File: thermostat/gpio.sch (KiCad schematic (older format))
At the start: 24 parts, among them J5 Conn_01x20, Q4 BC817, Q5 BC817, Q6 BC817, U8 PCF8574

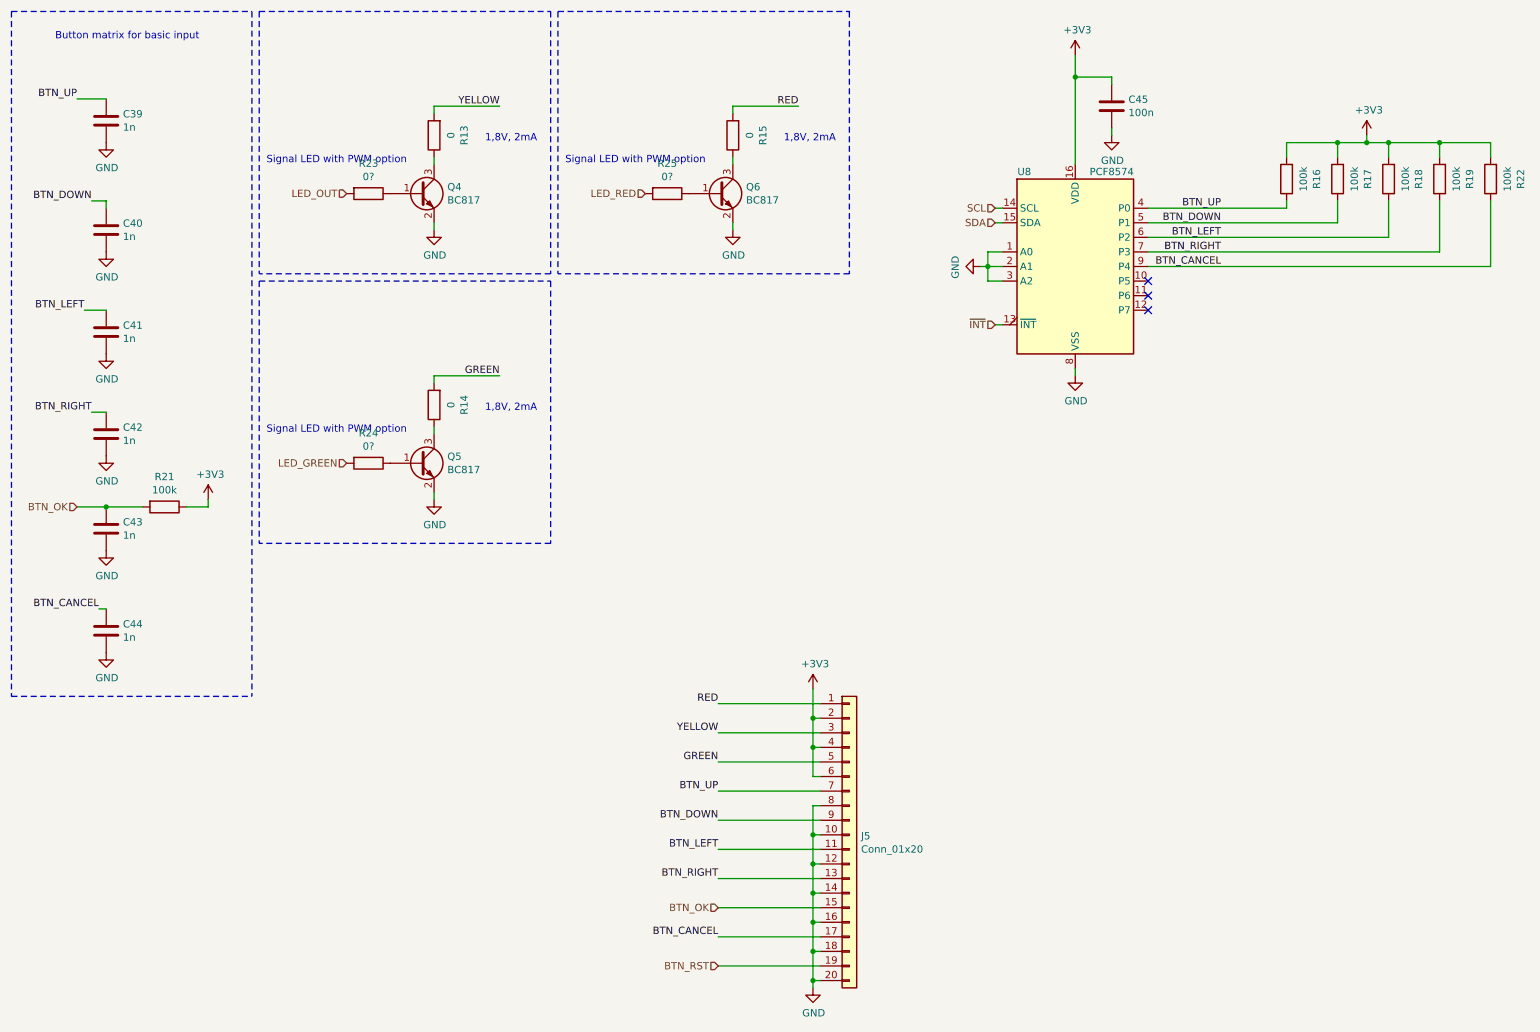
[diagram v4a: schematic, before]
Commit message: Changed LED and regulator_out drivers to NMOS instead of bipolar. Started routing, SPI and I2C lines done.
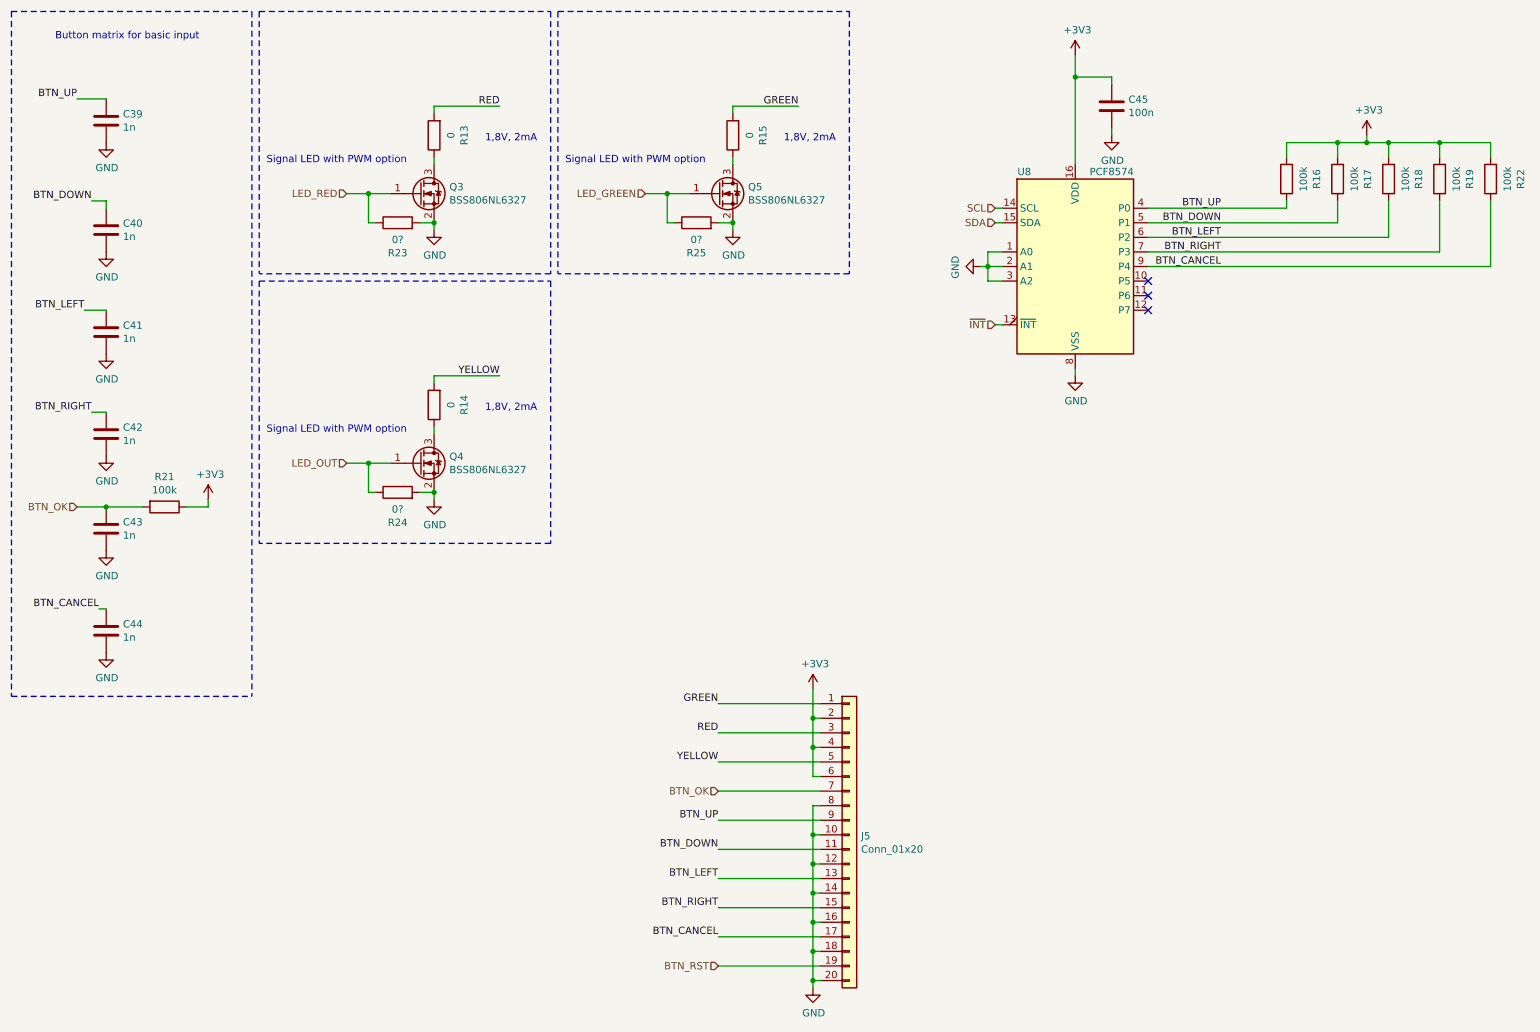
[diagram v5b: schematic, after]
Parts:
- removed Q4, Q5, Q6: BC817, Package_TO_SOT_SMD:SOT-23, symbol Device:Q_NPN_BEC
- added Q3, Q4, Q5: BSS806NL6327, Package_TO_SOT_SMD:SOT-23, symbol Device:Q_NMOS_GSD
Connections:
- net BTN_DOWN: now also J5.11 (Pin_11); no longer J5.9 (Pin_9)
- net BTN_LEFT: now also J5.13 (Pin_13); no longer J5.11 (Pin_11)
- net BTN_OK: now also J5.7 (Pin_7); no longer J5.15 (Pin_15)
- net BTN_RIGHT: now also J5.15 (Pin_15); no longer J5.13 (Pin_13)
- net BTN_UP: now also J5.9 (Pin_9); no longer J5.7 (Pin_7)
- net GND: now also R23.2, R24.2, R25.2, Q3.2 (S), Q4.2 (S), Q5.2 (S)
- net GREEN: now also J5.1 (Pin_1), R15.2; no longer J5.5 (Pin_5), R14.2
- net LED_GREEN: now also R25.1, Q5.1 (G); no longer R24.2
- net LED_OUT: now also R24.1, Q4.1 (G); no longer R23.2
- net LED_RED: now also R23.1, Q3.1 (G); no longer R25.2
- net RED: now also J5.3 (Pin_3), R13.2; no longer J5.1 (Pin_1), R15.2
- net YELLOW: now also J5.5 (Pin_5), R14.2; no longer J5.3 (Pin_3), R13.2
- net at R15.1: now also Q5.3 (D)
- net at R13.1: now also Q3.3 (D)
- net at R14.1: now also Q4.3 (D)
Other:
- moved on the sheet: R23, R24, R25
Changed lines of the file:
@@
 Text Notes 5950 1500 0    50   ~ 0
 1,8V, 2mA
-$Comp
-L Device:Q_NPN_BEC Q?
-U 1 1 5F3B8DF8
-P 5500 1850
-AR Path="/5E6A63AE/5F3B8DF8" Ref="Q?"  Part="1"
-AR Path="/5F3B8DF8" Ref="Q?"  Part="1"
-AR Path="/5F39C8C1/5F3B8DF8" Ref="Q6"  Part="1"
-F 0 "Q6" H 5691 1896 50  0000 L CNN
-F 1 "BC817" H 5691 1805 50  0000 L CNN
-F 2 "Package_TO_SOT_SMD:SOT-23" H 5700 1950 50  0001 C CNN
-F 3 "https://www.mouser.de/datasheet/2/916/BC817_SER-1598763.pdf" H 5500 1850 50  0001 C CNN
-	1    5500 1850
-	1    0    0    -1
-$EndComp
 Wire Wire Line
 	5600 1600 5600 1650
@@
 Text Notes 3900 1500 0    50   ~ 0
 1,8V, 2mA
-$Comp
-L Device:Q_NPN_BEC Q?
-U 1 1 5F3B8E17
-P 3450 1850
-AR Path="/5E6A63AE/5F3B8E17" Ref="Q?"  Part="1"
-AR Path="/5F3B8E17" Ref="Q?"  Part="1"
-AR Path="/5F39C8C1/5F3B8E17" Ref="Q4"  Part="1"
-F 0 "Q4" H 3641 1896 50  0000 L CNN
-F 1 "BC817" H 3641 1805 50  0000 L CNN
-F 2 "Package_TO_SOT_SMD:SOT-23" H 3650 1950 50  0001 C CNN
-F 3 "https://www.mouser.de/datasheet/2/916/BC817_SER-1598763.pdf" H 3450 1850 50  0001 C CNN
-	1    3450 1850
-	1    0    0    -1
-$EndComp
 Wire Wire Line
 	3550 1600 3550 1650
@@
 Text Notes 3900 3350 0    50   ~ 0
 1,8V, 2mA
-$Comp
-L Device:Q_NPN_BEC Q?
-U 1 1 5F3B8E36
-P 3450 3700
-AR Path="/5E6A63AE/5F3B8E36" Ref="Q?"  Part="1"
-AR Path="/5F3B8E36" Ref="Q?"  Part="1"
-AR Path="/5F39C8C1/5F3B8E36" Ref="Q5"  Part="1"
-F 0 "Q5" H 3641 3746 50  0000 L CNN
-F 1 "BC817" H 3641 3655 50  0000 L CNN
-F 2 "Package_TO_SOT_SMD:SOT-23" H 3650 3800 50  0001 C CNN
-F 3 "https://www.mouser.de/datasheet/2/916/BC817_SER-1598763.pdf" H 3450 3700 50  0001 C CNN
-	1    3450 3700
-	1    0    0    -1
-$EndComp
 Wire Wire Line
 	3550 3450 3550 3500
@@
 Wire Notes Line
 	2350 600  2350 2400
+Text HLabel 2950 3700 0    50   Input ~ 0
+LED_OUT
 Text HLabel 2950 1850 0    50   Input ~ 0
-LED_OUT
+LED_RED
 Text HLabel 5000 1850 0    50   Input ~ 0
-LED_RED
-Text HLabel 2950 3700 0    50   Input ~ 0
 LED_GREEN
 Text Label 1100 1200 2    50   ~ 0
@@
 Wire Wire Line
 	5500 7150 6200 7150
+Text Label 5500 6750 2    50   ~ 0
+BTN_RIGHT
 Text Label 5500 6550 2    50   ~ 0
-BTN_RIGHT
+BTN_LEFT
 Text Label 5500 6350 2    50   ~ 0
-BTN_LEFT
+BTN_DOWN
 Text Label 5500 6150 2    50   ~ 0
-BTN_DOWN
-Text Label 5500 5950 2    50   ~ 0
 BTN_UP
 Text HLabel 5500 7150 0    50   Input ~ 0
@@
 Wire Wire Line
 	6200 5350 5500 5350
+Text Label 5500 5350 2    50   ~ 0
+GREEN
 Text Label 5500 5750 2    50   ~ 0
-GREEN
+YELLOW
 Text Label 5500 5550 2    50   ~ 0
-YELLOW
-Text Label 5500 5350 2    50   ~ 0
 RED
 $Comp
@@
 Wire Wire Line
 	3550 3100 4000 3100
+Text Label 4000 1250 2    50   ~ 0
+RED
+Text Label 4000 3100 2    50   ~ 0
+YELLOW
 Text Label 6050 1250 2    50   ~ 0
-RED
-Text Label 4000 1250 2    50   ~ 0
-YELLOW
-Text Label 4000 3100 2    50   ~ 0
 GREEN
 $Comp
@@
 Text HLabel 1100 4000 0    50   Input ~ 0
 BTN_OK
-Text HLabel 5500 6750 0    50   Input ~ 0
+Text HLabel 5500 5950 0    50   Input ~ 0
 BTN_OK
 Text Label 5500 6950 2    50   ~ 0
@@
 L Device:R R?
 U 1 1 5FAA9C4A
-P 3100 1850
+P 3300 2050
 AR Path="/5E6A63AE/5FAA9C4A" Ref="R?"  Part="1"
 AR Path="/5FAA9C4A" Ref="R?"  Part="1"
 AR Path="/5F39C8C1/5FAA9C4A" Ref="R23"  Part="1"
-F 0 "R23" V 2893 1850 50  0000 C CNN
-F 1 "0?" V 2984 1850 50  0000 C CNN
-F 2 "Resistor_SMD:R_0402_1005Metric" V 3030 1850 50  0001 C CNN
-F 3 "~" H 3100 1850 50  0001 C CNN
-	1    3100 1850
-	0    1    1    0
+F 0 "R23" V 3093 2050 50  0000 C CNN
+F 1 "0?" V 3184 2050 50  0000 C CNN
+F 2 "Resistor_SMD:R_0402_1005Metric" V 3230 2050 50  0001 C CNN
+F 3 "~" H 3300 2050 50  0001 C CNN
+	1    3300 2050
+	0    -1   -1   0
 $EndComp
 $Comp
 L Device:R R?
 U 1 1 5FAAA4F5
-P 5150 1850
+P 5350 2050
 AR Path="/5E6A63AE/5FAAA4F5" Ref="R?"  Part="1"
 AR Path="/5FAAA4F5" Ref="R?"  Part="1"
 AR Path="/5F39C8C1/5FAAA4F5" Ref="R25"  Part="1"
-F 0 "R25" V 4943 1850 50  0000 C CNN
-F 1 "0?" V 5034 1850 50  0000 C CNN
-F 2 "Resistor_SMD:R_0402_1005Metric" V 5080 1850 50  0001 C CNN
-F 3 "~" H 5150 1850 50  0001 C CNN
-	1    5150 1850
-	0    1    1    0
+F 0 "R25" V 5143 2050 50  0000 C CNN
+F 1 "0?" V 5234 2050 50  0000 C CNN
+F 2 "Resistor_SMD:R_0402_1005Metric" V 5280 2050 50  0001 C CNN
+F 3 "~" H 5350 2050 50  0001 C CNN
+	1    5350 2050
+	0    -1   -1   0
 $EndComp
 $Comp
 L Device:R R?
 U 1 1 5FAAA7FD
-P 3100 3700
+P 3300 3900
 AR Path="/5E6A63AE/5FAAA7FD" Ref="R?"  Part="1"
 AR Path="/5FAAA7FD" Ref="R?"  Part="1"
 AR Path="/5F39C8C1/5FAAA7FD" Ref="R24"  Part="1"
-F 0 "R24" V 2893 3700 50  0000 C CNN
-F 1 "0?" V 2984 3700 50  0000 C CNN
-F 2 "Resistor_SMD:R_0402_1005Metric" V 3030 3700 50  0001 C CNN
-F 3 "~" H 3100 3700 50  0001 C CNN
-	1    3100 3700
-	0    1    1    0
-$EndComp
+F 0 "R24" V 3093 3900 50  0000 C CNN
+F 1 "0?" V 3184 3900 50  0000 C CNN
+F 2 "Resistor_SMD:R_0402_1005Metric" V 3230 3900 50  0001 C CNN
+F 3 "~" H 3300 3900 50  0001 C CNN
+	1    3300 3900
+	0    -1   -1   0
+$EndComp
+$Comp
+L Device:Q_NMOS_GSD Q?
+U 1 1 5F792335
+P 3450 1850
+AR Path="/5E63CFCA/5F792335" Ref="Q?"  Part="1"
+AR Path="/5F792335" Ref="Q?"  Part="1"
+AR Path="/5F306ECC/5F792335" Ref="Q?"  Part="1"
+AR Path="/5F39C8C1/5F792335" Ref="Q3"  Part="1"
+F 0 "Q3" H 3655 1896 50  0000 L CNN
+F 1 "BSS806NL6327" H 3655 1805 50  0000 L CNN
+F 2 "Package_TO_SOT_SMD:SOT-23" H 3650 1950 50  0001 C CNN
+F 3 "~" H 3450 1850 50  0001 C CNN
+	1    3450 1850
+	1    0    0    -1
+$EndComp
+$Comp
+L Device:Q_NMOS_GSD Q?
+U 1 1 5F7963CB
+P 3450 3700
+AR Path="/5E63CFCA/5F7963CB" Ref="Q?"  Part="1"
+AR Path="/5F7963CB" Ref="Q?"  Part="1"
+AR Path="/5F306ECC/5F7963CB" Ref="Q?"  Part="1"
+AR Path="/5F39C8C1/5F7963CB" Ref="Q4"  Part="1"
+F 0 "Q4" H 3655 3746 50  0000 L CNN
+F 1 "BSS806NL6327" H 3655 3655 50  0000 L CNN
+F 2 "Package_TO_SOT_SMD:SOT-23" H 3650 3800 50  0001 C CNN
+F 3 "~" H 3450 3700 50  0001 C CNN
+	1    3450 3700
+	1    0    0    -1
+$EndComp
+$Comp
+L Device:Q_NMOS_GSD Q?
+U 1 1 5F796F73
+P 5500 1850
+AR Path="/5E63CFCA/5F796F73" Ref="Q?"  Part="1"
+AR Path="/5F796F73" Ref="Q?"  Part="1"
+AR Path="/5F306ECC/5F796F73" Ref="Q?"  Part="1"
+AR Path="/5F39C8C1/5F796F73" Ref="Q5"  Part="1"
+F 0 "Q5" H 5705 1896 50  0000 L CNN
+F 1 "BSS806NL6327" H 5705 1805 50  0000 L CNN
+F 2 "Package_TO_SOT_SMD:SOT-23" H 5700 1950 50  0001 C CNN
+F 3 "~" H 5500 1850 50  0001 C CNN
+	1    5500 1850
+	1    0    0    -1
+$EndComp
+Wire Wire Line
+	3450 2050 3550 2050
+Connection ~ 3550 2050
+Wire Wire Line
+	3250 1850 3100 1850
+Wire Wire Line
+	3150 2050 3100 2050
+Wire Wire Line
+	3100 2050 3100 1850
+Connection ~ 3100 1850
+Wire Wire Line
+	3100 1850 2950 1850
+Wire Wire Line
+	5500 2050 5600 2050
+Connection ~ 5600 2050
+Wire Wire Line
+	5300 1850 5150 1850
+Wire Wire Line
+	5200 2050 5150 2050
+Wire Wire Line
+	5150 2050 5150 1850
+Connection ~ 5150 1850
+Wire Wire Line
+	5150 1850 5000 1850
+Wire Wire Line
+	3450 3900 3550 3900
+Connection ~ 3550 3900
+Wire Wire Line
+	3250 3700 3100 3700
+Wire Wire Line
+	3150 3900 3100 3900
+Wire Wire Line
+	3100 3900 3100 3700
+Connection ~ 3100 3700
+Wire Wire Line
+	3100 3700 2950 3700
 $EndSCHEMATC

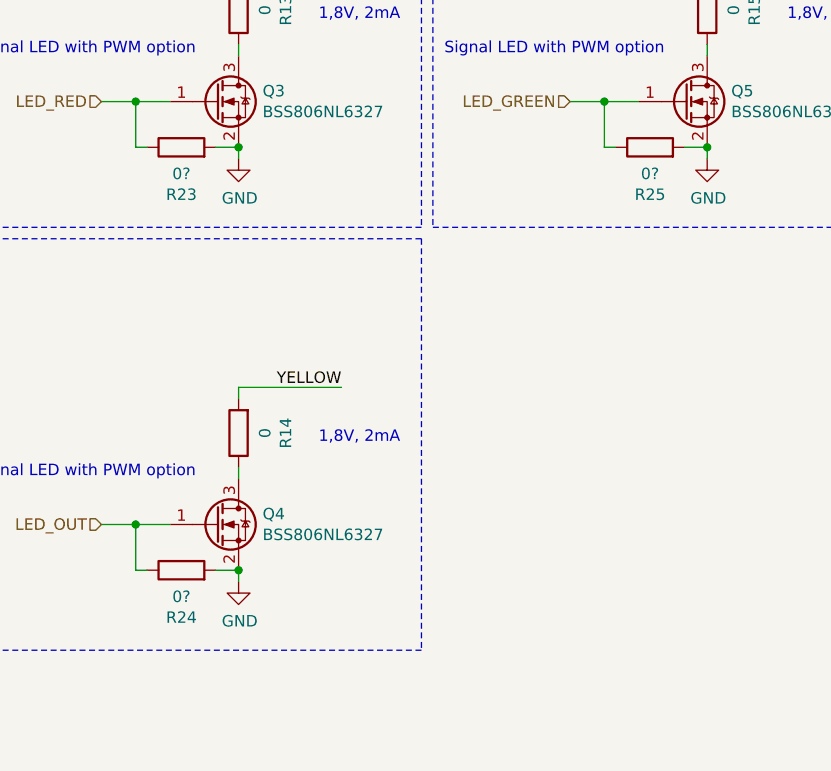
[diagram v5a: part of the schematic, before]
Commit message: Specified some resistor values.
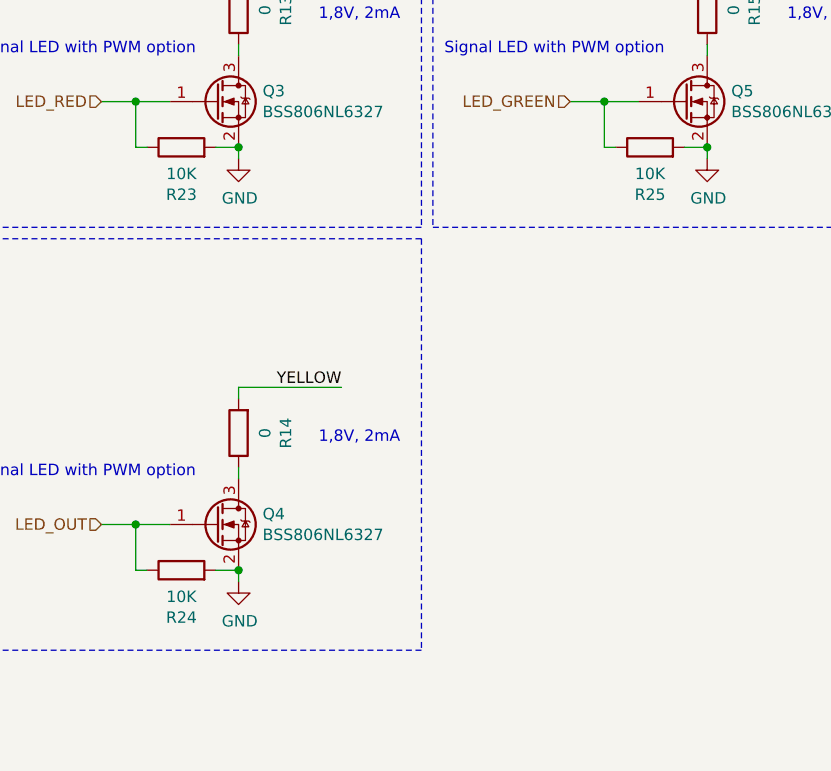
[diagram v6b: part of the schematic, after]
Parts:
- R23, R24, R25: value 0? -> 10K
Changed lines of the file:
@@
 AR Path="/5F39C8C1/5FAA9C4A" Ref="R23"  Part="1"
 F 0 "R23" V 3093 2050 50  0000 C CNN
-F 1 "0?" V 3184 2050 50  0000 C CNN
+F 1 "10K" V 3184 2050 50  0000 C CNN
 F 2 "Resistor_SMD:R_0402_1005Metric" V 3230 2050 50  0001 C CNN
 F 3 "~" H 3300 2050 50  0001 C CNN
@@
 AR Path="/5F39C8C1/5FAAA4F5" Ref="R25"  Part="1"
 F 0 "R25" V 5143 2050 50  0000 C CNN
-F 1 "0?" V 5234 2050 50  0000 C CNN
+F 1 "10K" V 5234 2050 50  0000 C CNN
 F 2 "Resistor_SMD:R_0402_1005Metric" V 5280 2050 50  0001 C CNN
 F 3 "~" H 5350 2050 50  0001 C CNN
@@
 AR Path="/5F39C8C1/5FAAA7FD" Ref="R24"  Part="1"
 F 0 "R24" V 3093 3900 50  0000 C CNN
-F 1 "0?" V 3184 3900 50  0000 C CNN
+F 1 "10K" V 3184 3900 50  0000 C CNN
 F 2 "Resistor_SMD:R_0402_1005Metric" V 3230 3900 50  0001 C CNN
 F 3 "~" H 3300 3900 50  0001 C CNN
